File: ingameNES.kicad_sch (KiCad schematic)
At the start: 7 parts, among them J1 SJ-43504-SMT-TR

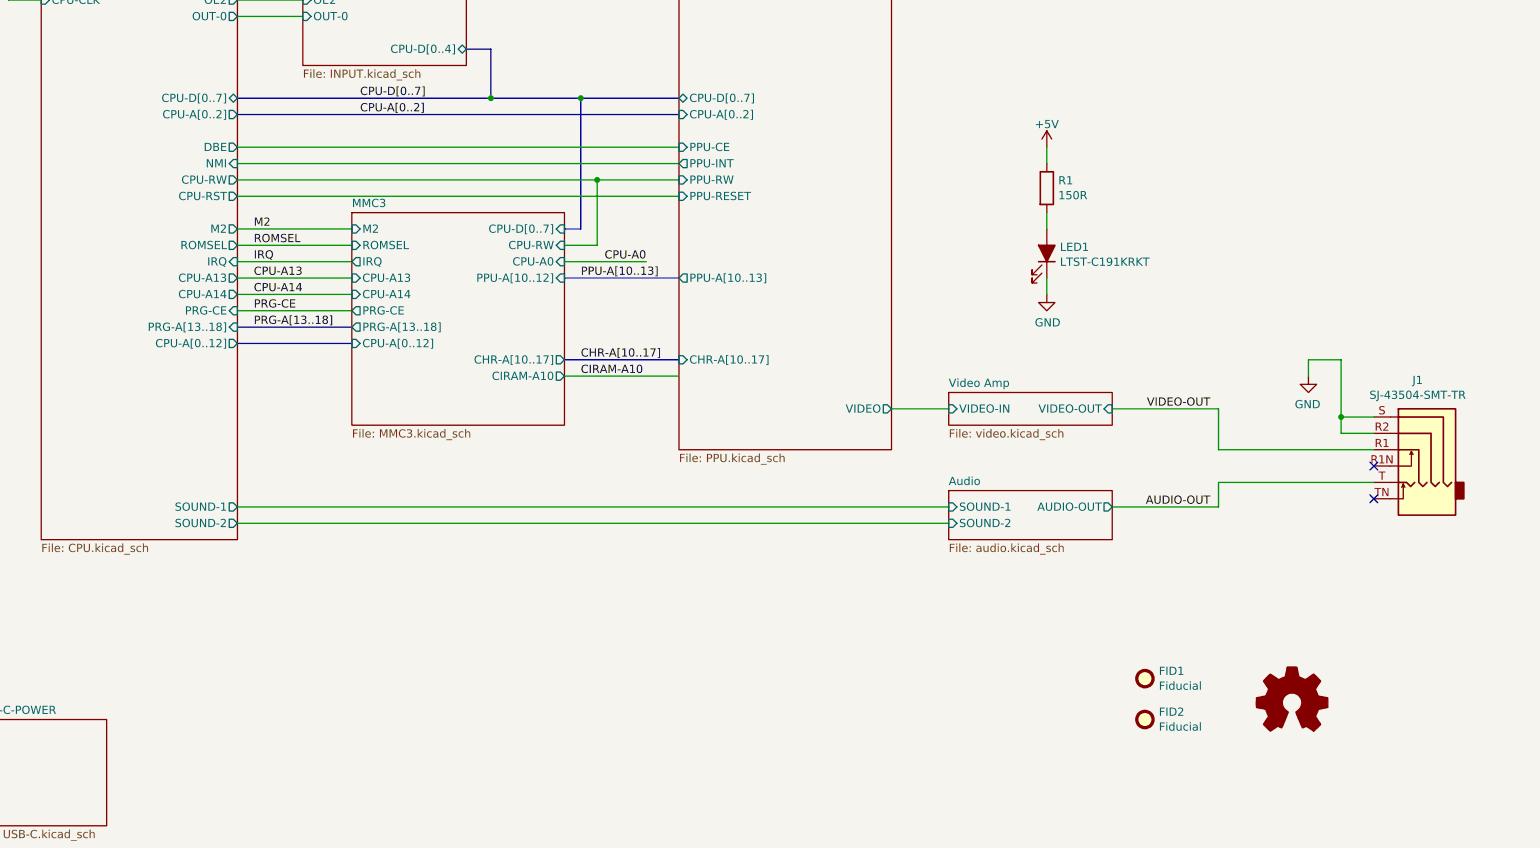
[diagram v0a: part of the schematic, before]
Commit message: rev2 sent to fab
Added CHR RAM.
Changed board to 4 layers (was 2 layers).
Changed passives to 0603 (was 0402)
Fixed CIRAM-A10 not being hooked up
Fixed PPU-A10..A12 being hooked to VRAM but should have been.
Added more silkscreen for easier debugging.
Added filter inductor to 5V from USB-C.
Changed video out to stock (was THS7374)
Changed audio circuit to stock (was headphone amp IC)
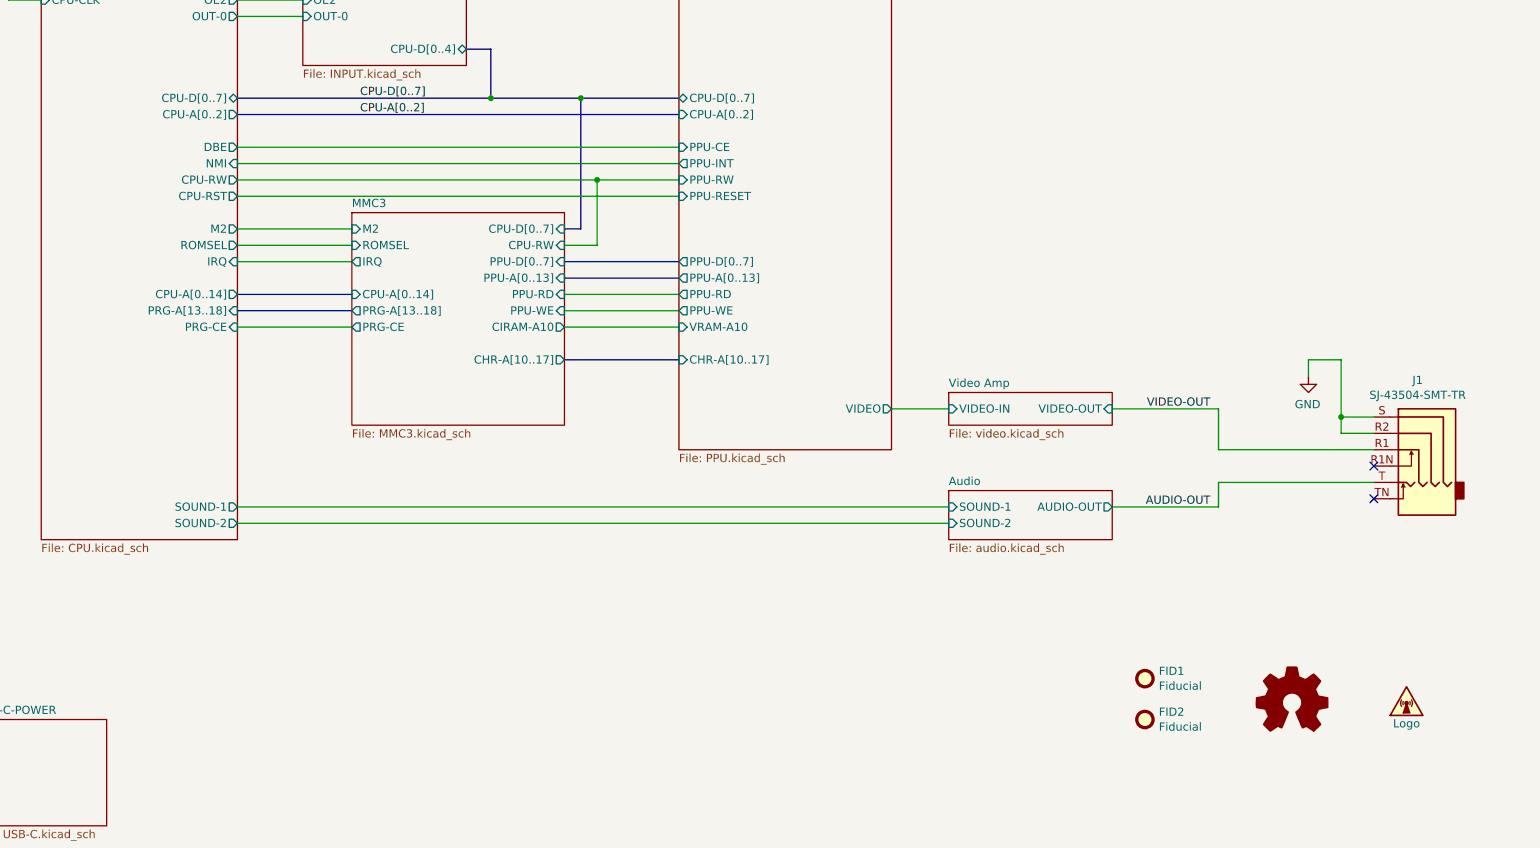
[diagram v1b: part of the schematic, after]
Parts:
- removed LED1: LTST-C191KRKT, LED_SMD:LED_0603_1608Metric, symbol Device:LED_Filled
- removed R1: 150R, Resistor_SMD:R_0603_1608Metric, symbol Device:R
- added SYM1: Logo, footprints:RCR_waitforme, symbol Graphic:SYM_Radio_Waves_Small
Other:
- sheet CPU ports: added CPU-A[0..14]; removed CPU-A13, CPU-A14, CPU-A[0..12]
- sheet MMC3 ports: added CPU-A[0..14], PPU-A[0..13], PPU-D[0..7], PPU-RD, PPU-WE; removed CPU-A0, CPU-A13, CPU-A14, CPU-A[0..12], PPU-A[10..12]
- sheet PPU ports: added PPU-A[0..13], PPU-D[0..7], PPU-RD, PPU-WE, VRAM-A10; removed PPU-A[10..13]

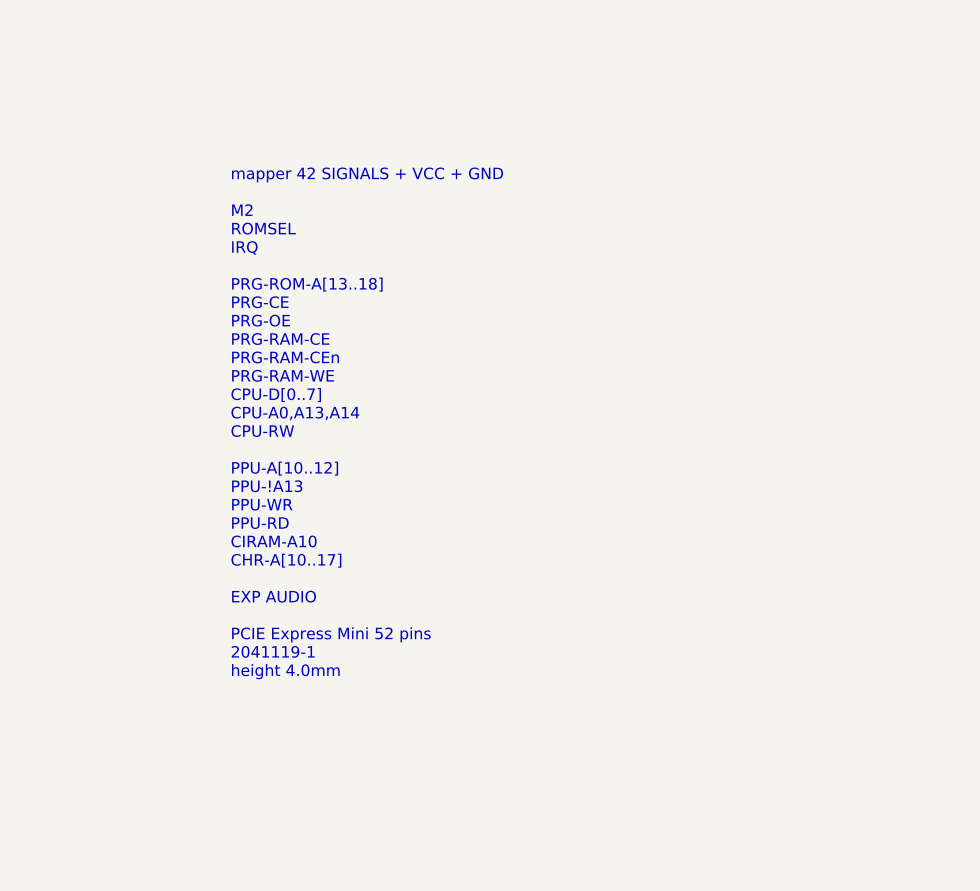
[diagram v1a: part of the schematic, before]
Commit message: filled out BOM
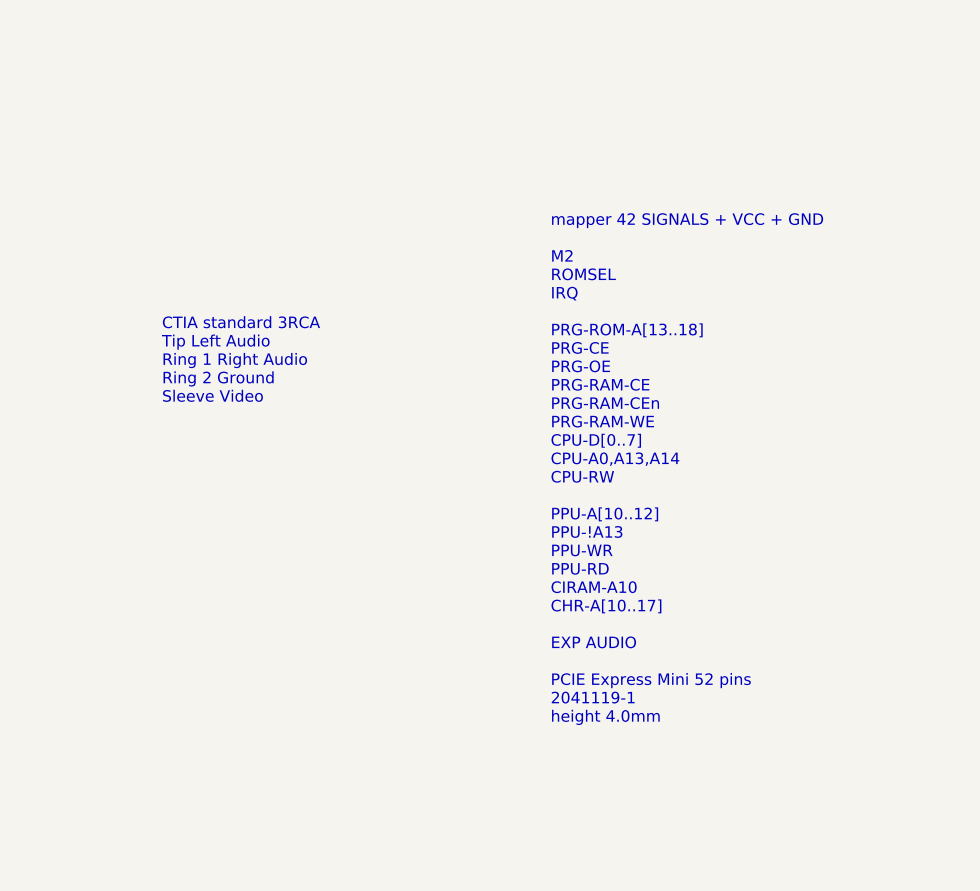
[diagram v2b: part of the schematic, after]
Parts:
- SYM1: now left out of the parts list
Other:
- note added: "CTIA standard 3RCA Tip Left Audio Ring 1 Right Audio Ring 2 Ground Sleeve Video"
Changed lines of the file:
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@@
   (title_block
     (title "InGame-NES MMC3")
-    (date "2022-06-03")
-    (rev "1")
+    (date "2022-08-02")
+    (rev "2")
     (company "Late to the Game")
   )
@@
   )
   (text "mapper 42 SIGNALS + VCC + GND\n\nM2\nROMSEL\nIRQ\n\nPRG-ROM-A[13..18]\nPRG-CE\nPRG-OE\nPRG-RAM-CE\nPRG-RAM-CEn\nPRG-RAM-WE\nCPU-D[0..7]\nCPU-A0,A13,A14\nCPU-RW\n\nPPU-A[10..12]\nPPU-!A13\nPPU-WR\nPPU-RD\nCIRAM-A10\nCHR-A[10..17]\n\nEXP AUDIO\n\nPCIE Express Mini 52 pins\n2041119-1\nheight 4.0mm"
-    (at 293.37 157.48 0)
+    (at 328.93 162.56 0)
+    (effects (font (size 1.27 1.27)) (justify left bottom))
+  )
+  (text "CTIA standard 3RCA\nTip Left Audio\nRing 1 Right Audio\nRing 2 Ground\nSleeve Video"
+    (at 285.75 127 0)
     (effects (font (size 1.27 1.27)) (justify left bottom))
   )
@@
   )
   (symbol (lib_id "Graphic:Logo_Open_Hardware_Small") (at 231.14 162.56 0) (unit 1)
-    (in_bom no) (on_board yes)
+    (in_bom no) (on_board no)
     (property "Reference" "#LOGO1" (id 0) (at 231.14 155.575 0)
       (effects (font (size 1.27 1.27)) hide)
@@
   )
   (symbol (lib_id "Graphic:SYM_Radio_Waves_Small") (at 248.92 162.56 0) (unit 1)
-    (in_bom yes) (on_board yes) (fields_autoplaced)
+    (in_bom no) (on_board yes) (fields_autoplaced)
     (property "Reference" "SYM1" (id 0) (at 248.92 159.004 0)
       (effects (font (size 1.27 1.27)) hide)
@@
       (reference "#C2") (unit 1) (value "330p") (footprint "Capacitor_SMD:C_0402_1005Metric")
     )
-    (path "/00000000-0000-0000-0000-0000602e4b45/fdb89b58-2166-4574-89a2-dad8c17edf7a"
-      (reference "#C3") (unit 1) (value "100n") (footprint "Capacitor_SMD:C_0402_1005Metric")
-    )
     (path "/00000000-0000-0000-0000-00006076ea7e/9b75adf3-d9a1-4436-9b23-0c65f231ab46"
       (reference "#C4") (unit 1) (value "330p") (footprint "Capacitor_SMD:C_0402_1005Metric")
@@
       (reference "#C36") (unit 1) (value "51p") (footprint "Capacitor_SMD:C_0402_1005Metric")
     )
-    (path "/00000000-0000-0000-0000-0000602e4b45/00000000-0000-0000-0000-0000619c71c8"
-      (reference "#C48") (unit 1) (value "100n") (footprint "Capacitor_SMD:C_0402_1005Metric")
-    )
     (path "/00000000-0000-0000-0000-000061acc981"
       (reference "#H1") (unit 1) (value "MountingHole_M3") (footprint "MountingHole:MountingHole_3mm")
@@
       (reference "#PWR075") (unit 1) (value "GND") (footprint "")
     )
-    (path "/00000000-0000-0000-0000-0000602e4b45/00000000-0000-0000-0000-0000619c71bd"
-      (reference "#PWR080") (unit 1) (value "GND") (footprint "")
-    )
     (path "/00000000-0000-0000-0000-0000602e5cdc/00000000-0000-0000-0000-000061b0251b"
       (reference "#PWR0101") (unit 1) (value "GND") (footprint "")
@@
       (reference "#PWR0121") (unit 1) (value "GND") (footprint "")
     )
-    (path "/00000000-0000-0000-0000-0000602e4b45/04df1c58-4b47-4352-b8a5-046f653b60a7"
-      (reference "#PWR0122") (unit 1) (value "GND") (footprint "")
-    )
     (path "/00000000-0000-0000-0000-00006076ea7e/d3f06d28-d53d-4513-961b-af050f9d6bff"
       (reference "#PWR0123") (unit 1) (value "+5V") (footprint "")
@@
       (reference "#PWR0148") (unit 1) (value "+5V") (footprint "")
     )
-    (path "/00000000-0000-0000-0000-0000602e4b45/00000000-0000-0000-0000-000061bf163c"
-      (reference "#PWR0149") (unit 1) (value "GND") (footprint "")
-    )
     (path "/00000000-0000-0000-0000-00006076ea7e/a920b7a1-5ff3-44a6-914e-17b5626e0d18"
       (reference "#PWR0150") (unit 1) (value "GND") (footprint "")
@@
       (reference "#PWR0168") (unit 1) (value "+5V") (footprint "")
     )
-    (path "/00000000-0000-0000-0000-0000602e4b45/00000000-0000-0000-0000-000061c01c59"
-      (reference "#PWR0169") (unit 1) (value "GND") (footprint "")
-    )
     (path "/00000000-0000-0000-0000-0000618b7f4d/8da195f3-d79c-49d5-b26b-8654efa09b3f"
       (reference "#PWR0170") (unit 1) (value "GND") (footprint "")
@@
       (reference "#PWR0190") (unit 1) (value "GND") (footprint "")
     )
-    (path "/00000000-0000-0000-0000-0000602e4b45/00000000-0000-0000-0000-000061b8b01a"
-      (reference "#PWR0191") (unit 1) (value "+5V") (footprint "")
-    )
     (path "/00000000-0000-0000-0000-0000618b7f4d/4011b300-ebeb-4301-a683-5c483a23fcbe"
       (reference "#PWR0192") (unit 1) (value "+5V") (footprint "")
@@
       (reference "#PWR0210") (unit 1) (value "GND") (footprint "")
     )
-    (path "/00000000-0000-0000-0000-0000602e4b45/12a8cd01-51f5-447c-8a4d-e5db488f215a"
-      (reference "#PWR0211") (unit 1) (value "+5V") (footprint "")
-    )
     (path "/00000000-0000-0000-0000-0000618b7f4d/4c503fea-1ffb-4af3-8c31-0ff1f99104b0"
       (reference "#PWR0212") (unit 1) (value "GND") (footprint "")
@@
       (reference "#PWR0228") (unit 1) (value "+5V") (footprint "")
     )
-    (path "/00000000-0000-0000-0000-0000602e4b45/0f872c40-ef1a-4280-a19e-659457432ed4"
-      (reference "#PWR0230") (unit 1) (value "GND") (footprint "")
-    )
-    (path "/00000000-0000-0000-0000-0000602e4b45/aae131c8-82ae-414a-b3b8-c7621145f108"
-      (reference "#PWR0231") (unit 1) (value "GND") (footprint "")
-    )
-    (path "/00000000-0000-0000-0000-0000602e4b45/7c100d13-66cb-46b2-beab-f9e35dc66013"
-      (reference "#PWR0232") (unit 1) (value "+5V") (footprint "")
-    )
-    (path "/00000000-0000-0000-0000-0000602e4b45/11acf68e-b267-4635-86b8-6f03c2c91aff"
-      (reference "#PWR0233") (unit 1) (value "GND") (footprint "")
-    )
     (path "/00000000-0000-0000-0000-00006076ea7e/6dba6c38-c4be-4c12-95a0-1407d4b23787"
       (reference "#PWR0234") (unit 1) (value "+5V") (footprint "")
@@
       (reference "#R8") (unit 1) (value "150K") (footprint "Resistor_SMD:R_0402_1005Metric")
     )
-    (path "/00000000-0000-0000-0000-0000602e4b45/e4f08b08-160d-4154-95b4-5ba892f1bed9"
-      (reference "#R9") (unit 1) (value "10K") (footprint "Resistor_SMD:R_0402_1005Metric")
-    )
     (path "/00000000-0000-0000-0000-000061b7ae74/00000000-0000-0000-0000-000061b85c85"
       (reference "#R10") (unit 1) (value "75R") (footprint "Resistor_SMD:R_0603_1608Metric_Pad0.98x0.95mm_HandSolder")
@@
       (reference "#U1") (unit 1) (value "NES-MMC3-DIP") (footprint "Package_DIP:DIP-40_W15.24mm_Socket")
     )
-    (path "/00000000-0000-0000-0000-0000602e4b45/e5d6cd7a-eb15-4eb2-bce9-5b40cdf4a5d0"
-      (reference "#U2") (unit 1) (value "FM18W08-SG") (footprint "footprints:SOIC-28W_7.5_8.7mm")
-    )
-    (path "/00000000-0000-0000-0000-0000602e4b45/2d2d419a-28fd-46e1-9440-bbc68dd5d7bf"
-      (reference "#U3") (unit 1) (value "74HC04") (footprint "")
-    )
-    (path "/00000000-0000-0000-0000-0000602e4b45/ed888618-45a8-44bd-9891-4453dbc5a503"
-      (reference "#U3") (unit 2) (value "74HC04") (footprint "")
-    )
-    (path "/00000000-0000-0000-0000-0000602e4b45/b29f0a07-701e-4dcd-b99e-83ab670ca5a4"
-      (reference "#U4") (unit 1) (value "74HC00") (footprint "")
-    )
     (path "/00000000-0000-0000-0000-0000618b7f4d/00000000-0000-0000-0000-000061d4dded"
       (reference "#U5") (unit 1) (value "74LS377") (footprint "")
@@
       (reference "#U7") (unit 3) (value "SN74HC32N") (footprint "Package_DIP:DIP-14_W7.62mm")
     )
-    (path "/00000000-0000-0000-0000-0000602e4b45/2d6d77e4-e3f4-40df-a31e-423cbf7449fa"
-      (reference "#U8") (unit 3) (value "74AHC04") (footprint "")
-    )
     (path "/00000000-0000-0000-0000-000060a9ace1/00000000-0000-0000-0000-000061f685f5"
       (reference "#U9") (unit 1) (value "SN74LVC1404DCT") (footprint "Package_SO:SSOP-8_2.95x2.8mm_P0.65mm")
     )
-    (path "/00000000-0000-0000-0000-0000602e4b45/00000000-0000-0000-0000-000061c366a7"
-      (reference "#U10") (unit 1) (value "IS62C256AL-45TLI") (footprint "footprints:TSOP-I-28_11.8x8mm_P0.55mm_ISSI")
-    )
-    (path "/00000000-0000-0000-0000-0000602e4b45/78bd3887-fdc4-4e9a-acd1-e467b76bd693"
-      (reference "#U11") (unit 2) (value "74HC00") (footprint "")
-    )
     (path "/00000000-0000-0000-0000-0000618b7f4d/00000000-0000-0000-0000-000061b1a2ff"
